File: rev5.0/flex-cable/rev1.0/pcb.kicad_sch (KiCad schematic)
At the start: 2 parts, among them J1 fpc, J2 oled

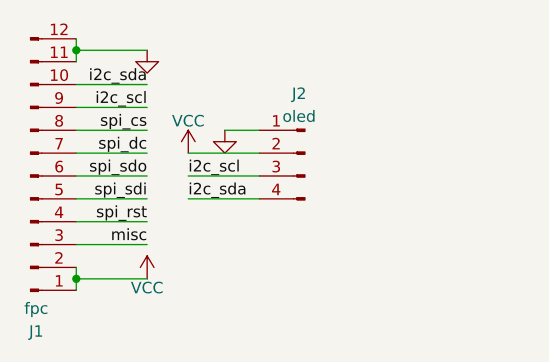
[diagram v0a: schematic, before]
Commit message: fix flex and expose GPIOs
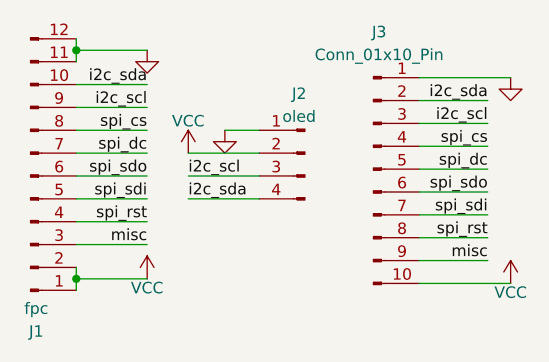
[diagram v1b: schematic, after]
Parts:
- added J3: Conn_01x10_Pin, Connector_PinHeader_2.54mm:PinHeader_1x10_P2.54mm_Vertical, symbol Connector:Conn_01x10_Pin
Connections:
- net GND: now also J3.1 (Pin_1)
- net VCC: now also J3.10 (Pin_10)
- net i2c_scl: now also J3.3 (Pin_3)
- net i2c_sda: now also J3.2 (Pin_2)
- net misc: now also J3.9 (Pin_9)
- net spi_cs: now also J3.4 (Pin_4)
- net spi_dc: now also J3.5 (Pin_5)
- net spi_rst: now also J3.8 (Pin_8)
- net spi_sdi: now also J3.7 (Pin_7)
- net spi_sdo: now also J3.6 (Pin_6)
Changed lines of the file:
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@@
+    (stroke (width 0) (type default))
+  )
+  (wire (pts (xy 193.04 130.81) (xy 182.88 130.81))
     (stroke (width 0) (type default))
   )
@@
     (stroke (width 0) (type default))
   )
+  (wire (pts (xy 190.5 110.49) (xy 182.88 110.49))
+    (stroke (width 0) (type default))
+  )
   (wire (pts (xy 144.78 113.792) (xy 152.654 113.792))
     (stroke (width 0) (type default))
   )
+  (wire (pts (xy 190.5 115.57) (xy 182.88 115.57))
+    (stroke (width 0) (type default))
+  )
+  (wire (pts (xy 190.5 113.03) (xy 182.88 113.03))
+    (stroke (width 0) (type default))
+  )
+  (wire (pts (xy 190.5 123.19) (xy 182.88 123.19))
+    (stroke (width 0) (type default))
+  )
+  (wire (pts (xy 193.04 107.95) (xy 182.88 107.95))
+    (stroke (width 0) (type default))
+  )
   (wire (pts (xy 144.78 130.302) (xy 144.78 131.572))
     (stroke (width 0) (type default))
@@
     (stroke (width 0) (type default))
   )
+  (wire (pts (xy 190.5 128.27) (xy 182.88 128.27))
+    (stroke (width 0) (type default))
+  )
   (wire (pts (xy 161.29 113.792) (xy 165.1 113.792))
     (stroke (width 0) (type default))
@@
     (stroke (width 0) (type default))
   )
+  (wire (pts (xy 190.5 125.73) (xy 182.88 125.73))
+    (stroke (width 0) (type default))
+  )
   (wire (pts (xy 144.78 104.902) (xy 152.654 104.902))
     (stroke (width 0) (type default))
@@
     (stroke (width 0) (type default))
   )
+  (wire (pts (xy 190.5 118.11) (xy 182.88 118.11))
+    (stroke (width 0) (type default))
+  )
   (wire (pts (xy 157.226 116.332) (xy 165.1 116.332))
     (stroke (width 0) (type default))
   )
+  (wire (pts (xy 190.5 120.65) (xy 182.88 120.65))
+    (stroke (width 0) (type default))
+  )
   (wire (pts (xy 157.226 121.412) (xy 165.1 121.412))
     (stroke (width 0) (type default))
+  )
+  (label "spi_sdo" (at 190.5 120.65 180) (fields_autoplaced)
+    (effects (font (size 1.27 1.27)) (justify right bottom))
+  )
+  (label "misc" (at 190.5 128.27 180) (fields_autoplaced)
+    (effects (font (size 1.27 1.27)) (justify right bottom))
   )
   (label "i2c_scl" (at 157.226 118.872 0) (fields_autoplaced)
@@
     (effects (font (size 1.27 1.27)) (justify right bottom))
   )
+  (label "i2c_sda" (at 190.5 110.49 180) (fields_autoplaced)
+    (effects (font (size 1.27 1.27)) (justify right bottom))
+  )
   (label "misc" (at 152.654 126.492 180) (fields_autoplaced)
+    (effects (font (size 1.27 1.27)) (justify right bottom))
+  )
+  (label "spi_sdi" (at 190.5 123.19 180) (fields_autoplaced)
+    (effects (font (size 1.27 1.27)) (justify right bottom))
+  )
+  (label "spi_rst" (at 190.5 125.73 180) (fields_autoplaced)
     (effects (font (size 1.27 1.27)) (justify right bottom))
   )
@@
     (effects (font (size 1.27 1.27)) (justify left bottom))
   )
+  (label "spi_cs" (at 190.5 115.57 180) (fields_autoplaced)
+    (effects (font (size 1.27 1.27)) (justify right bottom))
+  )
   (label "spi_sdi" (at 152.654 121.412 180) (fields_autoplaced)
     (effects (font (size 1.27 1.27)) (justify right bottom))
   )
   (label "i2c_scl" (at 152.654 111.252 180) (fields_autoplaced)
+    (effects (font (size 1.27 1.27)) (justify right bottom))
+  )
+  (label "i2c_scl" (at 190.5 113.03 180) (fields_autoplaced)
+    (effects (font (size 1.27 1.27)) (justify right bottom))
+  )
+  (label "spi_dc" (at 190.5 118.11 180) (fields_autoplaced)
     (effects (font (size 1.27 1.27)) (justify right bottom))
   )
@@
     )
   )
+  (symbol (lib_id "power:GND") (at 193.04 107.95 0) (unit 1)
+    (in_bom yes) (on_board yes) (dnp no) (fields_autoplaced)
+    (property "Reference" "#PWR06" (at 193.04 114.3 0)
+      (effects (font (size 1.27 1.27)) hide)
+    )
+    (property "Value" "GND" (at 193.04 113.284 0)
+      (effects (font (size 1.27 1.27)) hide)
+    )
+    (property "Footprint" "" (at 193.04 107.95 0)
+      (effects (font (size 1.27 1.27)) hide)
+    )
+    (property "Datasheet" "" (at 193.04 107.95 0)
+      (effects (font (size 1.27 1.27)) hide)
+    )
+    (pin "1")
+    (instances
+      (project "pcb"
+        (path "/59f16264-4fca-4d31-9679-edff70f988cd"
+          (reference "#PWR06") (unit 1)
+        )
+      )
+    )
+  )
+  (symbol (lib_id "power:VCC") (at 193.04 130.81 0) (unit 1)
+    (in_bom yes) (on_board yes) (dnp no)
+    (property "Reference" "#PWR05" (at 193.04 134.62 0)
+      (effects (font (size 1.27 1.27)) hide)
+    )
+    (property "Value" "VCC" (at 193.04 131.826 0)
+      (effects (font (size 1.27 1.27)))
+    )
+    (property "Footprint" "" (at 193.04 130.81 0)
+      (effects (font (size 1.27 1.27)) hide)
+    )
+    (property "Datasheet" "" (at 193.04 130.81 0)
+      (effects (font (size 1.27 1.27)) hide)
+    )
+    (pin "1")
+    (instances
+      (project "pcb"
+        (path "/59f16264-4fca-4d31-9679-edff70f988cd"
+          (reference "#PWR05") (unit 1)
+        )
+      )
+    )
+  )
   (symbol (lib_id "power:GND") (at 161.29 113.792 0) (unit 1)
     (in_bom yes) (on_board yes) (dnp no) (fields_autoplaced)
@@
         )
       )
+    )
+  )
+  (symbol (lib_id "Connector:Conn_01x10_Pin") (at 177.8 118.11 0) (unit 1)
+    (in_bom yes) (on_board yes) (dnp no) (fields_autoplaced)
+    (property "Reference" "J3" (at 178.435 102.87 0)
+      (effects (font (size 1.27 1.27)))
+    )
+    (property "Value" "Conn_01x10_Pin" (at 178.435 105.41 0)
+      (effects (font (size 1.27 1.27)))
+    )
+    (property "Footprint" "Connector_PinHeader_2.54mm:PinHeader_1x10_P2.54mm_Vertical" (at 177.8 118.11 0)
+      (effects (font (size 1.27 1.27)) hide)
+    )
+    (property "Datasheet" "~" (at 177.8 118.11 0)
+      (effects (font (size 1.27 1.27)) hide)
+    )
+    (pin "1")
+    (pin "10")
+    (pin "2")
+    (pin "3")
+    (pin "4")
+    (pin "5")
+    (pin "6")
+    (pin "7")
+    (pin "8")
+    (pin "9")
+    (instances
+      (project "pcb"
+        (path "/59f16264-4fca-4d31-9679-edff70f988cd"
+          (reference "J3") (unit 1)
+        )
+      )
